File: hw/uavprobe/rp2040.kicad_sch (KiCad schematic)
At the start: 29 parts, among them SW1 SW_Push, U1 RP2040, U2 NCP1117-5.0_SOT223, U3 W25Q16JVSS, Y1 ABLS-12.000MHZ-B4-T

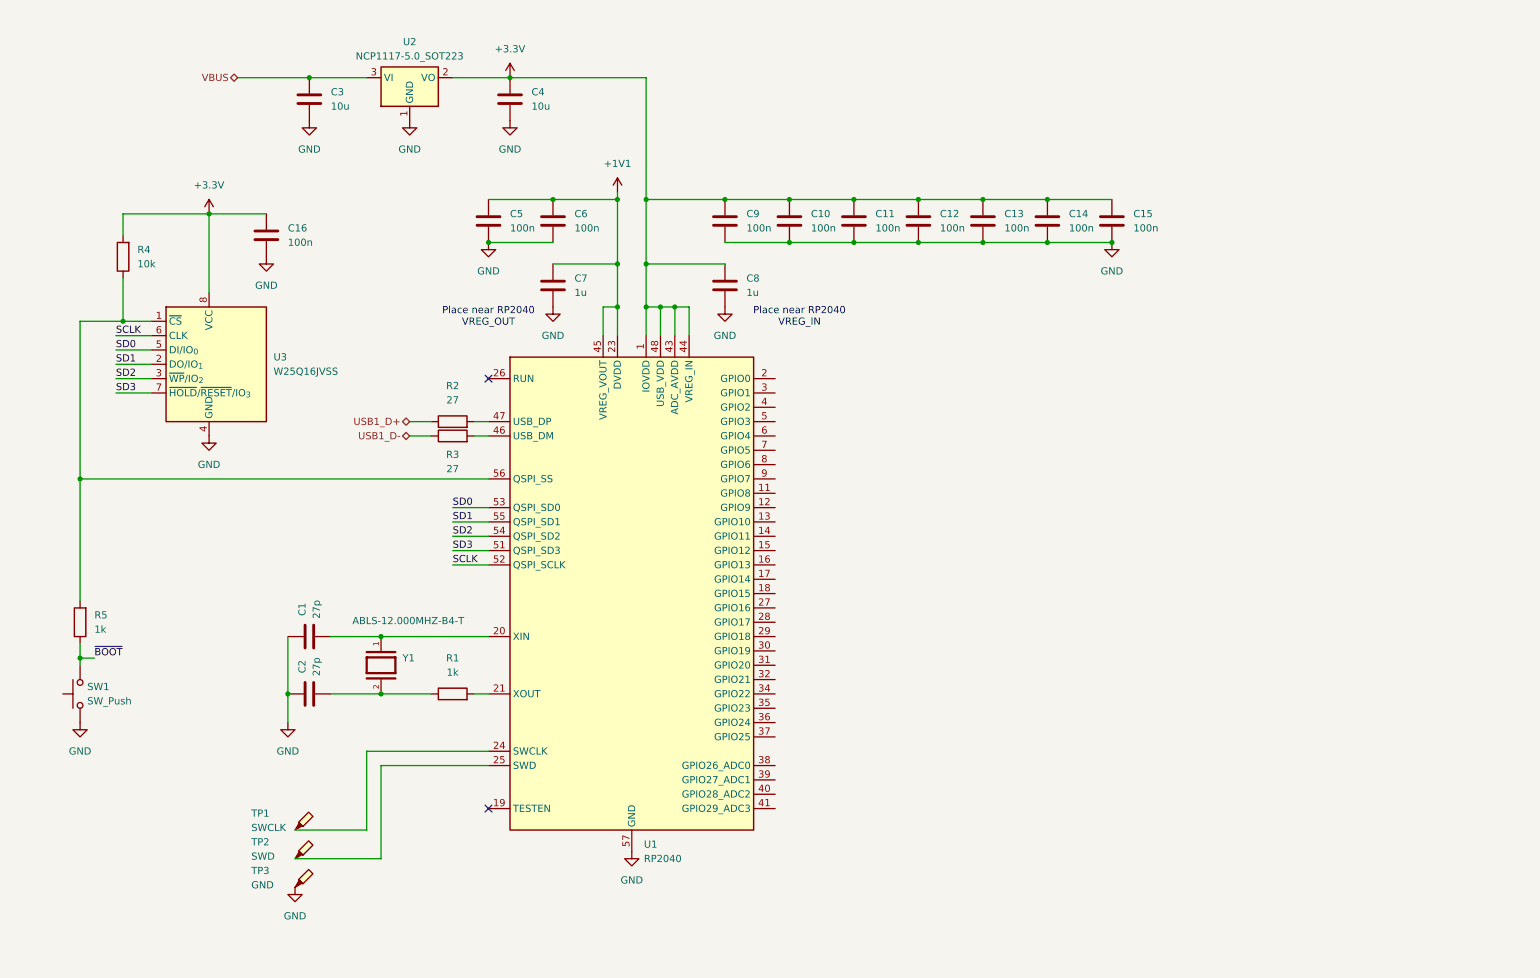
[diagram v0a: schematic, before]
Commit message: Connectors sheet and CAN/ESD
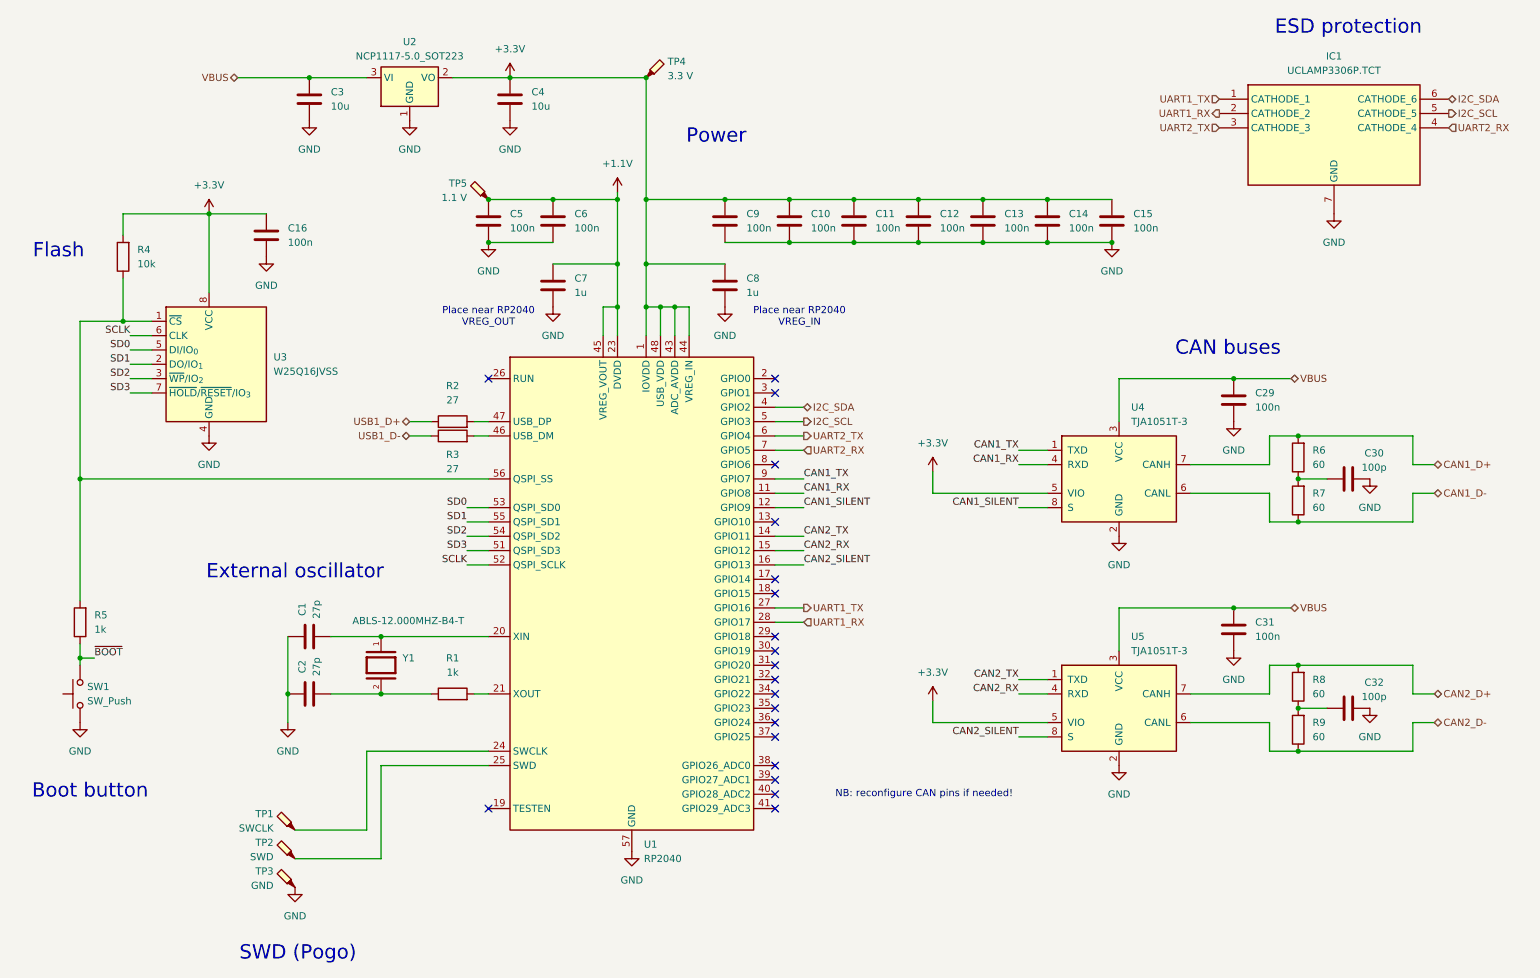
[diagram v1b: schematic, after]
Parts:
- added C29, C31: 100n, symbol Device:C
- added C30, C32: 100p, symbol Device:C
- added IC1: UCLAMP3306P.TCT, SON50P160X160X65-7N, symbol UCLAMP330:UCLAMP3306P.TCT
- added R6, R7, R8, R9: 60, symbol Device:R
- added TP4: 3.3 V, symbol Connector:TestPoint_Probe
- added TP5: 1.1 V, symbol Connector:TestPoint_Probe
- added U4, U5: TJA1051T-3, Package_SO:SOIC-8_3.9x4.9mm_P1.27mm, symbol Interface_CAN_LIN:TJA1051T-3
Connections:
- net +3.3V: now also TP4.1, U4.5 (VIO), U5.5 (VIO)
- net GND: now also C29.2, C30.1, C31.2, C32.1, IC1.7 (GND), U4.2 (GND), U5.2 (GND)
- net VBUS: now also C29.1, C31.1, U4.3 (VCC), U5.3 (VCC)
- net CAN1_RX: now reaches U1.11 (GPIO8)
- net CAN1_RX: now also U4.4 (RXD)
- net CAN1_SILENT: now reaches U1.12 (GPIO9)
- net CAN1_SILENT: now also U4.8 (S)
- net CAN2_TX: now reaches U1.14 (GPIO11)
- net CAN2_TX: now also U5.1 (TXD)
- net CAN2_RX: now reaches U1.15 (GPIO12)
- net CAN2_RX: now also U5.4 (RXD)
- net CAN2_SILENT: now reaches U1.16 (GPIO13)
- net CAN2_SILENT: now also U5.8 (S)
- net UART1_TX: now reaches U1.27 (GPIO16)
- net UART1_TX: now also IC1.1 (CATHODE_1)
- net UART1_RX: now reaches U1.28 (GPIO17)
- net UART1_RX: now also IC1.2 (CATHODE_2)
- net I2C_SDA: now reaches U1.4 (GPIO2)
- net I2C_SDA: now also IC1.6 (CATHODE_6)
- net I2C_SCL: now reaches U1.5 (GPIO3)
- net I2C_SCL: now also IC1.5 (CATHODE_5)
- net UART2_TX: now reaches U1.6 (GPIO4)
- net UART2_TX: now also IC1.3 (CATHODE_3)
- net UART2_RX: now reaches U1.7 (GPIO5)
- net UART2_RX: now also IC1.4 (CATHODE_4)
- net CAN1_TX: now reaches U1.9 (GPIO7)
- net CAN1_TX: now also U4.1 (TXD)
- net +1V1 renamed +1.1V
- net +1.1V: now also TP5.1
- new net: C32.2, R8.1, R9.2
- new net: C30.2, R6.1, R7.2
- new net CAN1_D+: R6.2, U4.7 (CANH)
- new net CAN1_D-: R7.1, U4.6 (CANL)
- new net CAN2_D+: R8.2, U5.7 (CANH)
- new net CAN2_D-: R9.1, U5.6 (CANL)
- no-connect marks 2 -> 20
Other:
- note added: "Boot button"
- note added: "CAN buses"
- note added: "ESD protection"
- note added: "External oscillator"
- note added: "Flash"
- note added: "NB: reconfigure CAN pins if needed!"
- note added: "Power"
- note added: "SWD (Pogo)"

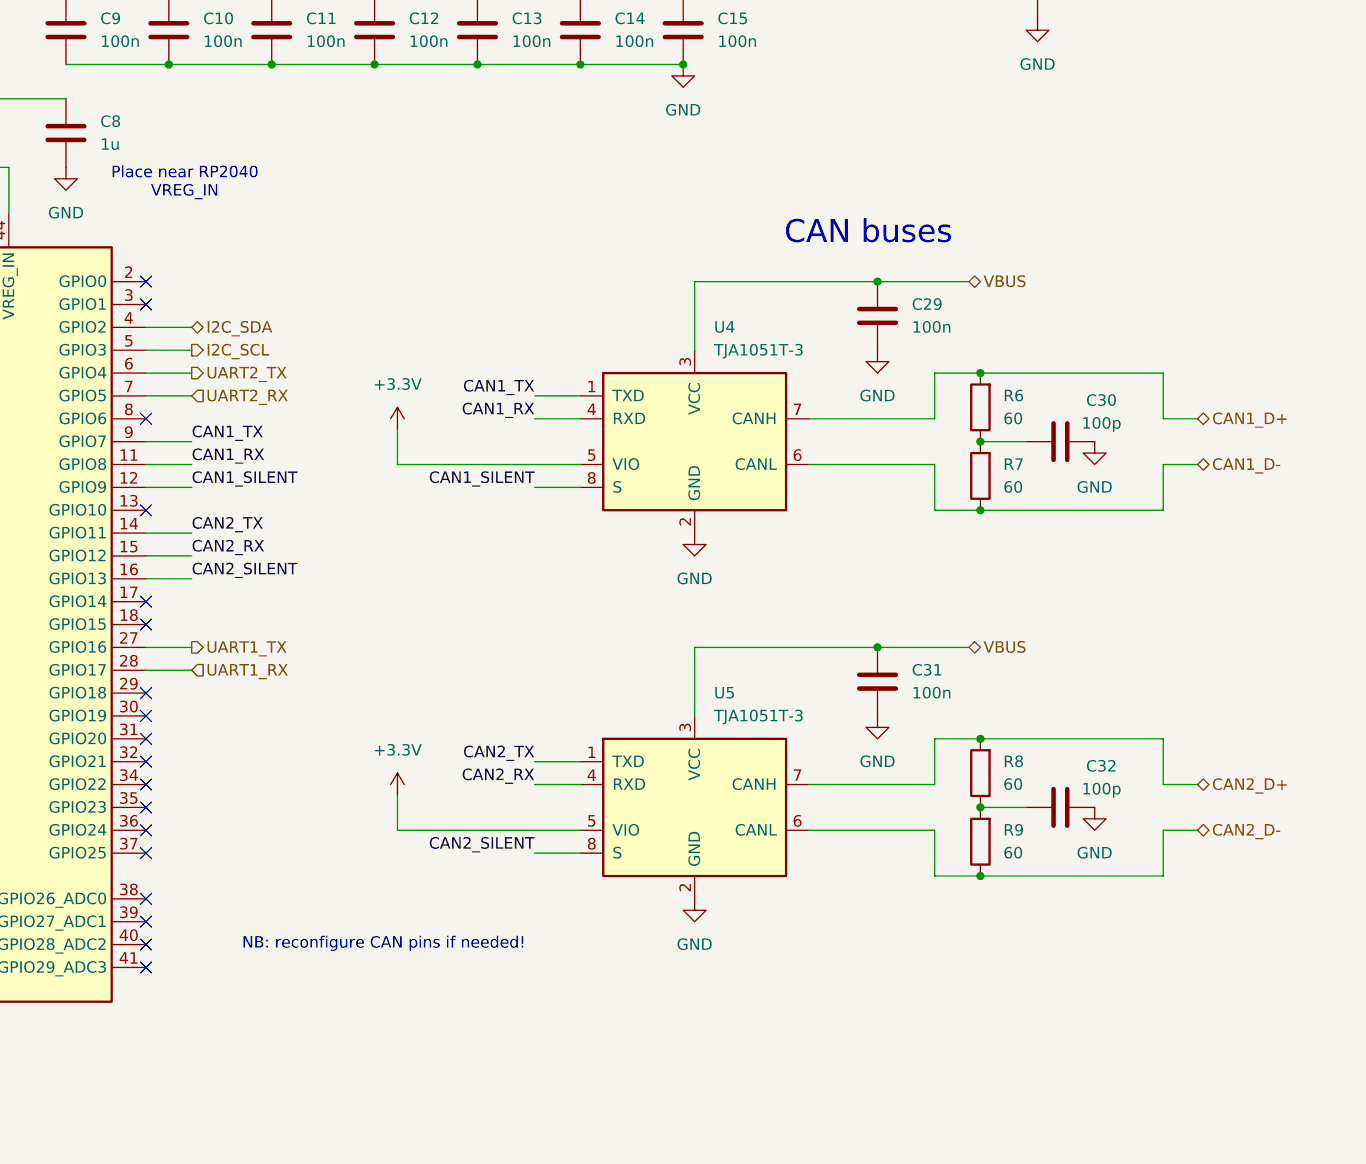
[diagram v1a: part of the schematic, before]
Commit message: CAN ESD protection
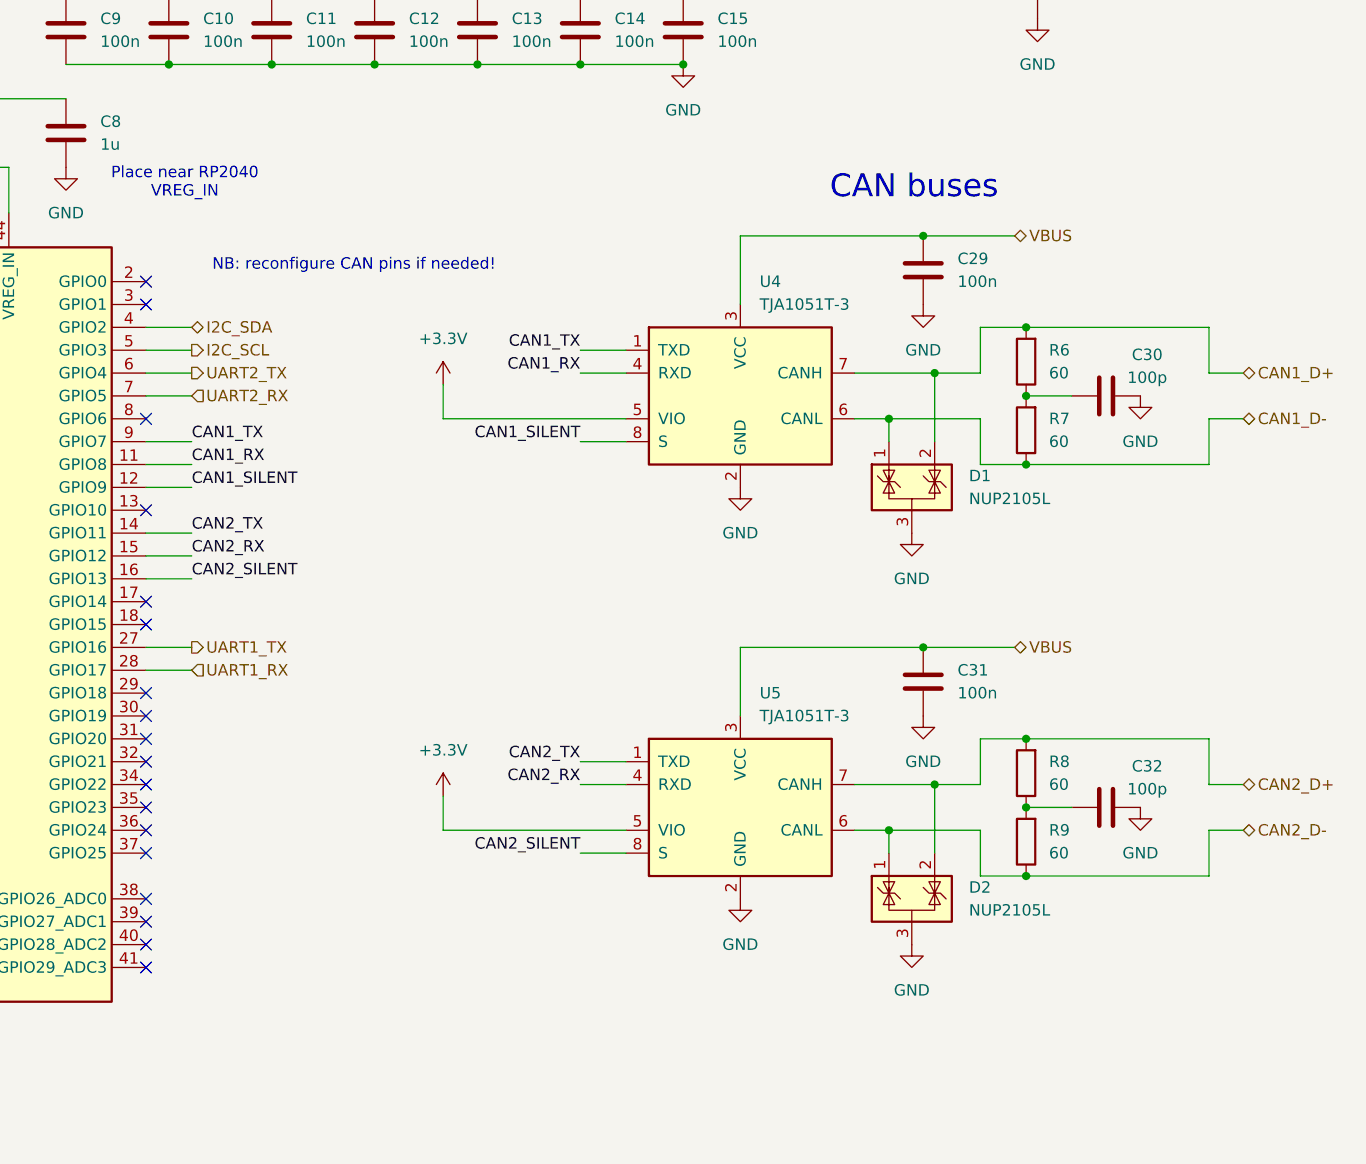
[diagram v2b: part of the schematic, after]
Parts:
- added D1, D2: NUP2105L, Package_TO_SOT_SMD:SOT-23, symbol Power_Protection:NUP2105L
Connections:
- net CAN1_D+: now also D1.2 (K)
- net CAN1_D-: now also D1.1 (K)
- net CAN2_D+: now also D2.2 (K)
- net CAN2_D-: now also D2.1 (K)
- net GND: now also D1.3 (A), D2.3 (A)
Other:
- moved on the sheet: C29, C30, C31, C32, R6, R7, R8, R9, U4, U5

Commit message: USB sheet
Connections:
- net VBUS renamed VBUS1
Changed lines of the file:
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@@
 		)
 	)
-	(hierarchical_label "VBUS"
+	(hierarchical_label "VBUS1"
 		(shape bidirectional)
 		(at 245.11 76.2 0)
@@
 		)
 	)
-	(hierarchical_label "VBUS"
+	(hierarchical_label "VBUS1"
 		(shape bidirectional)
 		(at 53.34 27.94 180)
@@
 		)
 	)
-	(hierarchical_label "VBUS"
+	(hierarchical_label "VBUS1"
 		(shape bidirectional)
 		(at 245.11 121.92 0)

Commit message: Cleanup and root sheet
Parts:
- renumbered C16 to C1, C8 to C10, C10 to C11, C11 to C12, C12 to C13, C13 to C14, C14 to C15, C15 to C16, C29 to C17, C31 to C18, C30 to C19, C3 to C2, C32 to C20, C1 to C3, C2 to C4, C4 to C6, C6 to C7, C7 to C8, R5 to R1, R4 to R2, R2 to R3, R3 to R4, R1 to R5, TP5 to TP4, TP4 to TP5, U3 to U1, U1 to U3
